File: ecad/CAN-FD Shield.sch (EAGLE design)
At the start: 39 parts, among them J2 JUMPER-3P-SHORT, J3 JUMPER-3P-SHORT, J4 JUMPER-3P-SHORT, J5 JUMPER-3P-SHORT, Q1 BSS123, U5 MCP2517FD, U6 MCP2542, X2 20MHz

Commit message: failure generator added to hardware design
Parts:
- added R2: 100k, rcl:R-EU_R0603
- Q1: value BSS123 -> FDV303
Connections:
- new net SOF: R1.1, U5.CLKO/SOF
- net GND: now also R2.1
- net IO7: now also R2.2
- net RX_CAN: no longer R1.1
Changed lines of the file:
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@@
 <part name="C1" library="Discrete-new" deviceset="CAP" device="-1206" value="22uF"/>
 <part name="R1" library="rcl" deviceset="R-EU_" device="R0603" value="0"/>
-<part name="Q1" library="transistor-small-signal" deviceset="BSS123" device=""/>
+<part name="Q1" library="transistor-small-signal" deviceset="BSS123" device="" value="FDV303"/>
 <part name="U$2" library="Power or GND " deviceset="GND_POWER" device=""/>
+<part name="R2" library="rcl" deviceset="R-EU_" device="R0603" value="100k"/>
+<part name="U$3" library="Power or GND " deviceset="GND_POWER" device=""/>
 </parts>
 <sheets>
@@
 <instance part="R1" gate="G$1" x="58.42" y="-12.7"/>
 <instance part="Q1" gate="G$1" x="104.14" y="-17.78"/>
-<instance part="U$2" gate="G$1" x="104.14" y="-25.4"/>
+<instance part="U$2" gate="G$1" x="104.14" y="-33.02"/>
+<instance part="R2" gate="G$1" x="96.52" y="-27.94" rot="R90"/>
+<instance part="U$3" gate="G$1" x="96.52" y="-33.02"/>
 </instances>
 <busses>
@@
 <pinref part="Q1" gate="G$1" pin="S"/>
 <pinref part="U$2" gate="G$1" pin="GND"/>
-<wire x1="104.14" y1="-25.4" x2="104.14" y2="-22.86" width="0.1524" layer="91"/>
+<wire x1="104.14" y1="-33.02" x2="104.14" y2="-22.86" width="0.1524" layer="91"/>
+</segment>
+<segment>
+<pinref part="R2" gate="G$1" pin="1"/>
+<pinref part="U$3" gate="G$1" pin="GND"/>
 </segment>
 </net>
@@
 <wire x1="104.14" y1="-12.7" x2="104.14" y2="-10.16" width="0.1524" layer="91"/>
 <wire x1="104.14" y1="-10.16" x2="116.84" y2="-10.16" width="0.1524" layer="91"/>
-<label x="114.3" y="-7.62" size="1.778" layer="95"/>
+<label x="116.84" y="-10.16" size="1.778" layer="95" xref="yes"/>
 </segment>
 </net>
@@
 <pinref part="U6" gate="G$1" pin="RXD"/>
 <wire x1="106.68" y1="50.8" x2="116.84" y2="50.8" width="0.1524" layer="91"/>
-</segment>
-<segment>
-<pinref part="R1" gate="G$1" pin="1"/>
-<wire x1="53.34" y1="-12.7" x2="45.72" y2="-12.7" width="0.1524" layer="91"/>
-<label x="40.64" y="-10.16" size="1.778" layer="95"/>
 </segment>
 </net>
@@
 <segment>
 <wire x1="90.17" y1="132.08" x2="82.55" y2="132.08" width="0.1524" layer="91"/>
-<label x="83.82" y="132.08" size="1.778" layer="95"/>
+<label x="90.17" y="132.08" size="0.889" layer="95" xref="yes"/>
 <pinref part="U4" gate="SEEEDUINO" pin="PD7/D7"/>
 </segment>
 <segment>
 <pinref part="Q1" gate="G$1" pin="G"/>
-<wire x1="99.06" y1="-20.32" x2="91.44" y2="-20.32" width="0.1524" layer="91"/>
-<label x="88.9" y="-17.78" size="1.778" layer="95"/>
+<wire x1="99.06" y1="-20.32" x2="96.52" y2="-20.32" width="0.1524" layer="91"/>
+<label x="91.44" y="-20.32" size="1.778" layer="95" rot="R180" xref="yes"/>
+<pinref part="R2" gate="G$1" pin="2"/>
+<wire x1="96.52" y1="-20.32" x2="91.44" y2="-20.32" width="0.1524" layer="91"/>
+<wire x1="96.52" y1="-22.86" x2="96.52" y2="-20.32" width="0.1524" layer="91"/>
+<junction x="96.52" y="-20.32"/>
 </segment>
 </net>
@@
 <segment>
 <wire x1="90.17" y1="121.92" x2="82.55" y2="121.92" width="0.1524" layer="91"/>
-<label x="83.82" y="121.92" size="1.778" layer="95"/>
+<label x="90.17" y="121.92" size="0.889" layer="95" xref="yes"/>
 <pinref part="U4" gate="SEEEDUINO" pin="PD3/D3/INT1/PWM"/>
 </segment>
@@
 <pinref part="R1" gate="G$1" pin="2"/>
 <wire x1="63.5" y1="-12.7" x2="71.12" y2="-12.7" width="0.1524" layer="91"/>
-<label x="68.58" y="-10.16" size="1.778" layer="95"/>
+<label x="71.12" y="-12.7" size="1.778" layer="95" xref="yes"/>
 </segment>
 </net>
@@
 </segment>
 </net>
+<net name="SOF" class="0">
+<segment>
+<label x="24.384" y="55.88" size="0.889" layer="95" rot="R180" xref="yes"/>
+<pinref part="U5" gate="G$1" pin="CLKO/SOF"/>
+<wire x1="29.21" y1="55.88" x2="24.384" y2="55.88" width="0.1524" layer="91"/>
+</segment>
+<segment>
+<pinref part="R1" gate="G$1" pin="1"/>
+<wire x1="53.34" y1="-12.7" x2="45.72" y2="-12.7" width="0.1524" layer="91"/>
+<label x="45.72" y="-12.7" size="1.778" layer="95" rot="R180" xref="yes"/>
+</segment>
+</net>

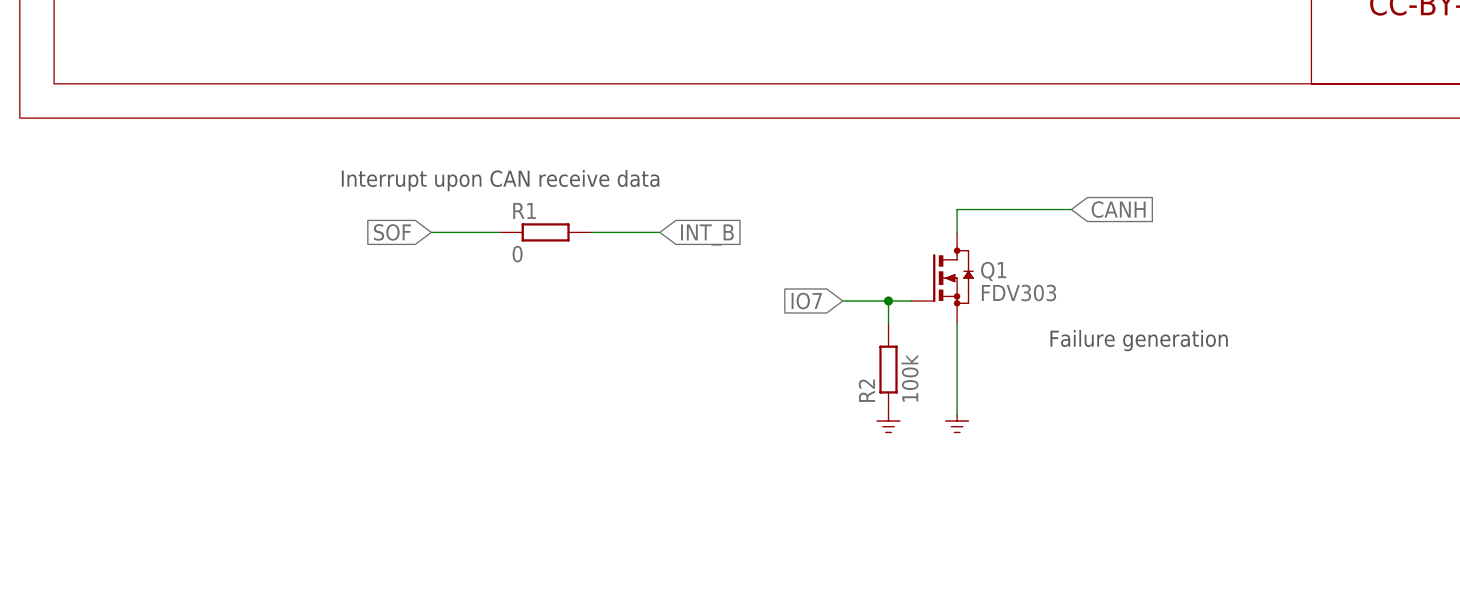
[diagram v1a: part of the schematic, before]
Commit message: Failure generation completed
Documentation updated
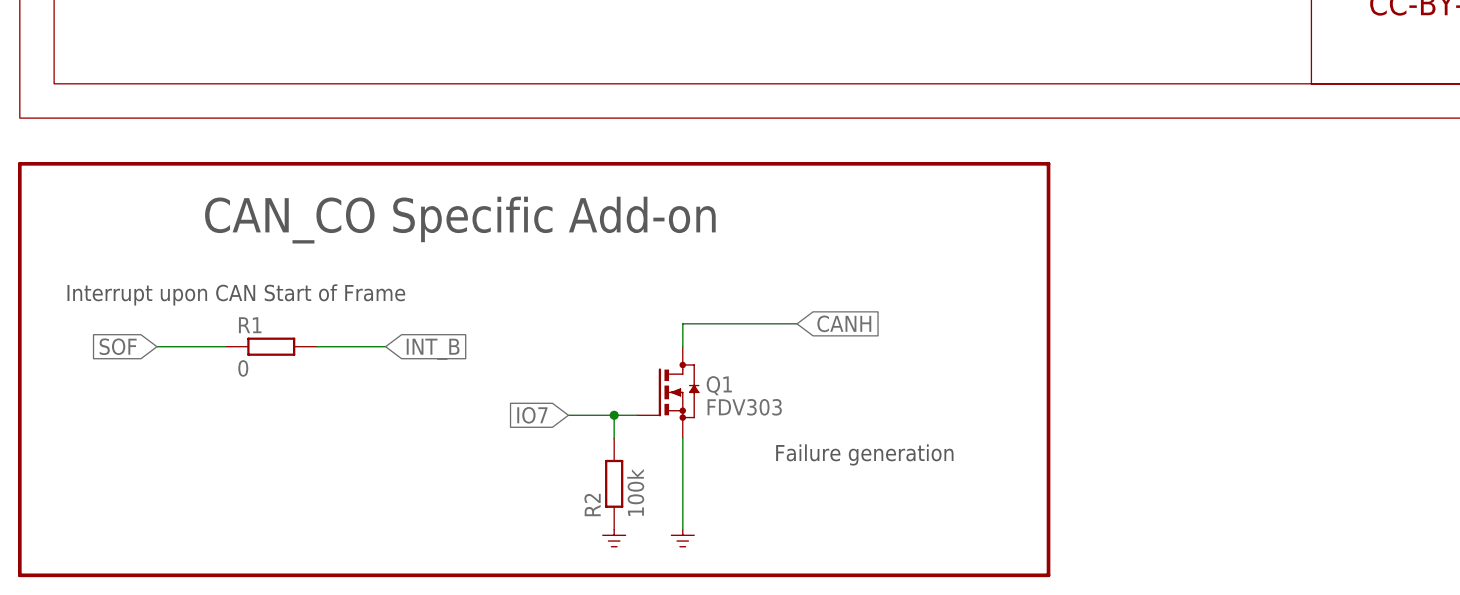
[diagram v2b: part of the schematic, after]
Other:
- note added: "CAN_CO Specific Add-on"
- note added: "Interrupt upon CAN Start of Frame"
- note removed: "Interrupt upon CAN receive data"
- moved on the sheet: Q1, R1, R2
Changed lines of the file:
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@@
 <text x="190.5" y="119.38" size="3.81" layer="97" ratio="10">TF_CARD</text>
 <text x="180.34" y="74.93" size="3.81" layer="97" ratio="10">LED</text>
-<text x="114.3" y="-25.4" size="1.778" layer="97">Failure generation</text>
-<text x="35.56" y="-7.62" size="1.778" layer="97">Interrupt upon CAN receive data</text>
+<text x="83.82" y="-38.1" size="1.778" layer="97">Failure generation</text>
+<text x="5.08" y="-20.32" size="1.778" layer="97">Interrupt upon CAN Start of Frame</text>
+<wire x1="0" y1="-5.08" x2="114.3" y2="-5.08" width="0.4064" layer="94"/>
+<wire x1="114.3" y1="-5.08" x2="114.3" y2="-50.8" width="0.4064" layer="94"/>
+<wire x1="114.3" y1="-50.8" x2="0" y2="-50.8" width="0.4064" layer="94"/>
+<wire x1="0" y1="-50.8" x2="0" y2="-5.08" width="0.4064" layer="94"/>
+<text x="20.32" y="-12.7" size="3.81" layer="97">CAN_CO Specific Add-on</text>
 </plain>
 <instances>
@@
 <instance part="J6" gate="G$1" x="110.49" y="157.48"/>
 <instance part="C1" gate="C" x="215.9" y="147.32" rot="R90"/>
-<instance part="R1" gate="G$1" x="58.42" y="-12.7"/>
-<instance part="Q1" gate="G$1" x="104.14" y="-17.78"/>
-<instance part="U$2" gate="G$1" x="104.14" y="-33.02"/>
-<instance part="R2" gate="G$1" x="96.52" y="-27.94" rot="R90"/>
-<instance part="U$3" gate="G$1" x="96.52" y="-33.02"/>
+<instance part="R1" gate="G$1" x="27.94" y="-25.4"/>
+<instance part="Q1" gate="G$1" x="73.66" y="-30.48"/>
+<instance part="U$2" gate="G$1" x="73.66" y="-45.72"/>
+<instance part="R2" gate="G$1" x="66.04" y="-40.64" rot="R90"/>
+<instance part="U$3" gate="G$1" x="66.04" y="-45.72"/>
 </instances>
 <busses>
@@
 <pinref part="Q1" gate="G$1" pin="S"/>
 <pinref part="U$2" gate="G$1" pin="GND"/>
-<wire x1="104.14" y1="-33.02" x2="104.14" y2="-22.86" width="0.1524" layer="91"/>
+<wire x1="73.66" y1="-45.72" x2="73.66" y2="-35.56" width="0.1524" layer="91"/>
 </segment>
 <segment>
@@
 <segment>
 <pinref part="Q1" gate="G$1" pin="D"/>
-<wire x1="104.14" y1="-12.7" x2="104.14" y2="-10.16" width="0.1524" layer="91"/>
-<wire x1="104.14" y1="-10.16" x2="116.84" y2="-10.16" width="0.1524" layer="91"/>
-<label x="116.84" y="-10.16" size="1.778" layer="95" xref="yes"/>
+<wire x1="73.66" y1="-25.4" x2="73.66" y2="-22.86" width="0.1524" layer="91"/>
+<wire x1="73.66" y1="-22.86" x2="86.36" y2="-22.86" width="0.1524" layer="91"/>
+<label x="86.36" y="-22.86" size="1.778" layer="95" xref="yes"/>
 </segment>
 </net>
@@
 <segment>
 <pinref part="Q1" gate="G$1" pin="G"/>
-<wire x1="99.06" y1="-20.32" x2="96.52" y2="-20.32" width="0.1524" layer="91"/>
-<label x="91.44" y="-20.32" size="1.778" layer="95" rot="R180" xref="yes"/>
+<wire x1="68.58" y1="-33.02" x2="66.04" y2="-33.02" width="0.1524" layer="91"/>
+<label x="60.96" y="-33.02" size="1.778" layer="95" rot="R180" xref="yes"/>
 <pinref part="R2" gate="G$1" pin="2"/>
-<wire x1="96.52" y1="-20.32" x2="91.44" y2="-20.32" width="0.1524" layer="91"/>
-<wire x1="96.52" y1="-22.86" x2="96.52" y2="-20.32" width="0.1524" layer="91"/>
-<junction x="96.52" y="-20.32"/>
+<wire x1="66.04" y1="-33.02" x2="60.96" y2="-33.02" width="0.1524" layer="91"/>
+<wire x1="66.04" y1="-35.56" x2="66.04" y2="-33.02" width="0.1524" layer="91"/>
+<junction x="66.04" y="-33.02"/>
 </segment>
 </net>
@@
 <segment>
 <pinref part="R1" gate="G$1" pin="2"/>
-<wire x1="63.5" y1="-12.7" x2="71.12" y2="-12.7" width="0.1524" layer="91"/>
-<label x="71.12" y="-12.7" size="1.778" layer="95" xref="yes"/>
+<wire x1="33.02" y1="-25.4" x2="40.64" y2="-25.4" width="0.1524" layer="91"/>
+<label x="40.64" y="-25.4" size="1.778" layer="95" xref="yes"/>
 </segment>
 </net>
@@
 <segment>
 <pinref part="R1" gate="G$1" pin="1"/>
-<wire x1="53.34" y1="-12.7" x2="45.72" y2="-12.7" width="0.1524" layer="91"/>
-<label x="45.72" y="-12.7" size="1.778" layer="95" rot="R180" xref="yes"/>
-</segment>
-</net>
+<wire x1="22.86" y1="-25.4" x2="15.24" y2="-25.4" width="0.1524" layer="91"/>
+<label x="15.24" y="-25.4" size="1.778" layer="95" rot="R180" xref="yes"/>
+</segment>
+</net>
